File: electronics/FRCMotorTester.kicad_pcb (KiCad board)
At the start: 4 copper layers, 85.6 x 70.8 mm, 108 parts, among them J1 USB_B_Micro, J2 Conn_01x02_Socket, J3 Conn_01x03, J4 Conn_01x03, J5 Conn_01x03, J6 Conn_01x03, J7 Conn_ARM_JTAG_SWD_10, J8 Conn_01x02, J9 Conn_01x08, Q2 IRLML6401, SW1 PTS645SK50SMTR92LFS, SW2 RotaryEncoder_Switch, SW3 RotaryEncoder_Switch, U1 STM32F415RGTx, U2 TCAN1043xDxQ1, U4 USBLC6-2SC6, U5 LM1117DT-ADJ, U6 AOZ1280CI, U7 LM1117DT-ADJ, Y2 Crystal_GND24

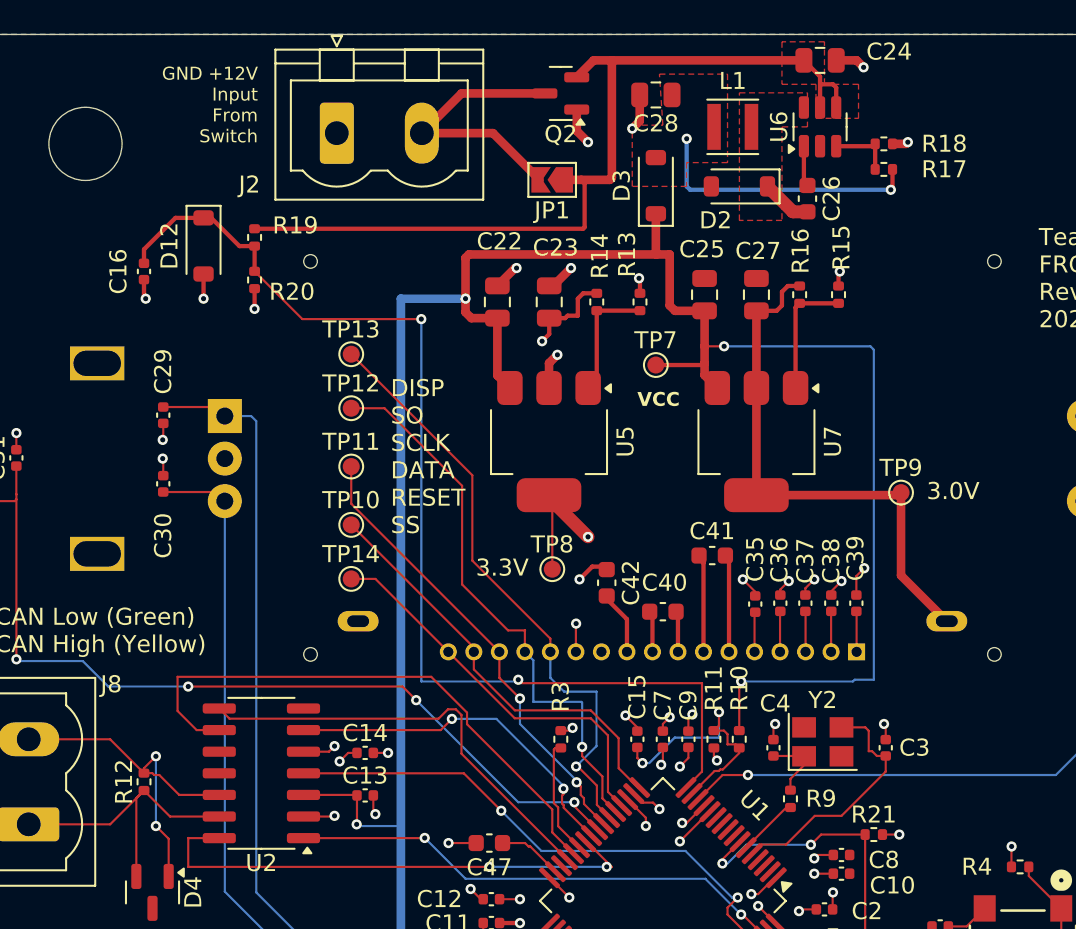
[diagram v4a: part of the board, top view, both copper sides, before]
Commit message: Tweaked parts to use Basic parts which are cheaper.
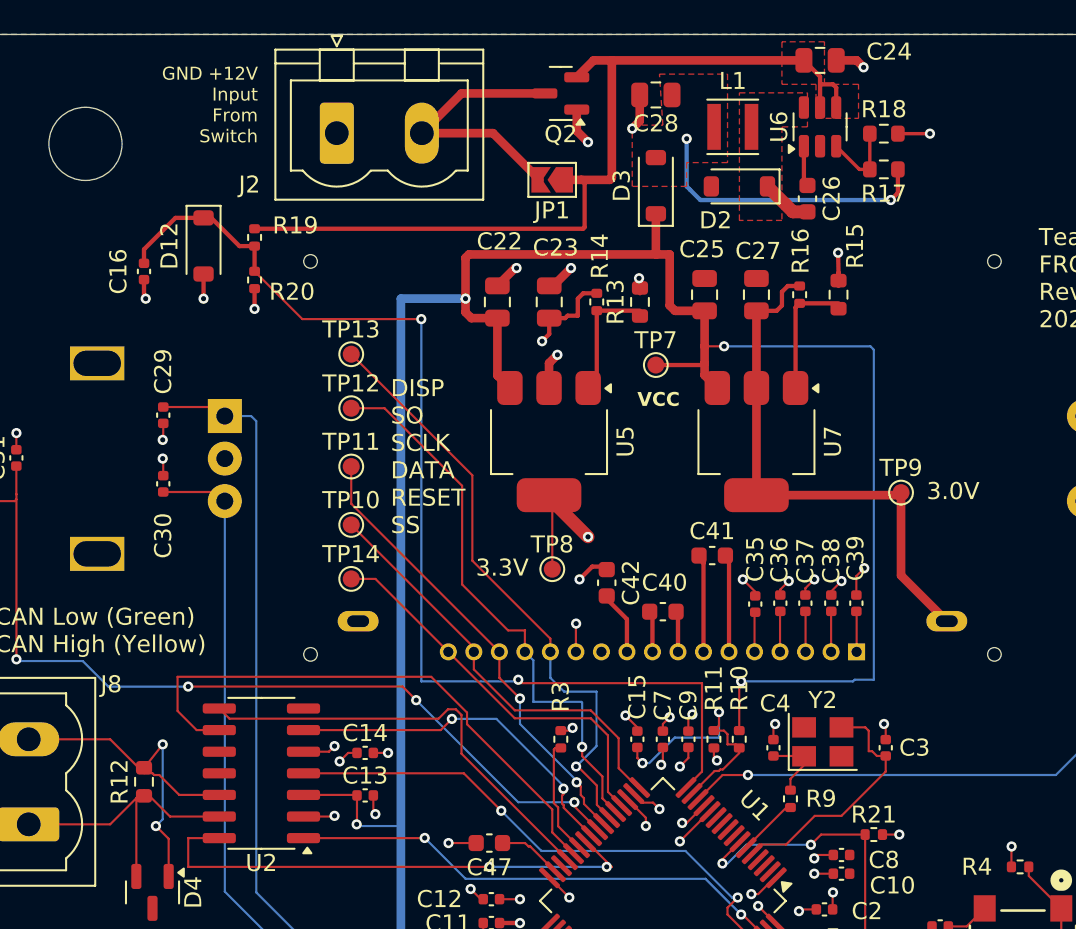
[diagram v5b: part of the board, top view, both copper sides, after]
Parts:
- R12, R13, R15, R17, R18: footprint Resistor_SMD:R_0402_1005Metric -> Resistor_SMD:R_0603_1608Metric
- moved R18 0.60 mm to (146.0, 41.9)
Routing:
- net GND: track 74.1 -> 76.1 mm
- net Net-(J8-Pin_2): track 21.2 -> 22.9 mm
- net Net-(D3-A): track 16.1 -> 17.1 mm
- net Net-(U6-FB): track 3.85 -> 4.64 mm

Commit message: Ordered this version.
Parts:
- SW1: footprint footprints:SW4_PTS645SK50SMTR92LFS_CNK -> footprints:PTS645SK50SMTR92LFS_CNK
- moved R4 2.50 mm to (154.0, 82.5)
- moved SW1 1.39 mm to (154.1, 89.3)
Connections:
- C17 pad 1: /Pico/BOOT -> BOOT
- DS1 pad 13: DISP_SO -> DISP_SI
- R2 pad 1: /Pico/BOOT -> BOOT
- SW1 pad 3: /Pico/BOOT -> BOOT
- SW1 pad 4: /Pico/BOOT -> BOOT
- TP13 pad 1: DISP_SO -> DISP_SI
- U1 pad 22: DISP_SO -> DISP_DATA
- U1 pad 23: DISP_DATA -> DISP_SI
- U1 pad 56: unconnected-(U1-PB4-Pad56) -> BOOT
- U1 pad 60: /Pico/BOOT -> BOOT
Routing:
- net DISP_SI: track 0.00 -> 36.0 mm, vias 0 -> 1
- net DISP_SO: track 35.7 -> 0.00 mm, vias 1 -> 0
- net BOOT: track 0.00 -> 30.2 mm
- net /Pico/BOOT: track 23.1 -> 0.00 mm
- net Net-(R4-Pad2): track 9.73 -> 14.1 mm

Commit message: Updated design for REV B.
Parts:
- removed C46: 2.2u, Capacitor_SMD:C_0603_1608Metric
- removed D7, D8: SP0502BAHT, Package_TO_SOT_SMD:SOT-23
- removed H2, H3, H4: MountingHole, MountingHole:MountingHole_4.3mm_M4
- removed J4, J5, J6: Conn_01x03, Connector_PinSocket_2.54mm:PinSocket_1x03_P2.54mm_Vertical
- removed J8: Conn_01x02, Connector_Phoenix_MSTB:PhoenixContact_MSTBVA_2,5_2-G_1x02_P5.00mm_Vertical
- removed U1: STM32F415RGTx, Package_QFP:LQFP-64_10x10mm_P0.5mm
- added J10: Conn_01x04, Connector_JST:JST_PH_S4B-PH-K_1x04_P2.00mm_Horizontal, F.Cu at (101.0, 43.5)
- added U3: STM32F446RETx, Package_QFP:LQFP-64_10x10mm_P0.5mm, F.Cu at (133.0, 87.0)
- C29, C30, C32, C33: value 0.1u -> 10n
- H1: footprint MountingHole:MountingHole_4.3mm_M4 -> footprints:brushless_buddy_logo
- J2: footprint Connector_Phoenix_MSTB:PhoenixContact_MSTBVA_2,5_2-G_1x02_P5.00mm_Vertical -> Connector_JST:JST_PH_S2B-PH-K_1x02_P2.00mm_Horizontal
- J3: value Conn_01x03 -> Conn_01x06; footprint Connector_PinSocket_2.54mm:PinSocket_1x03_P2.54mm_Vertical -> Connector_JST:JST_PH_S6B-PH-K_1x06_P2.00mm_Horizontal
- moved H1 91.5 mm to (169.2, 101.3)
- moved J3 32.0 mm to (167.7, 43.5), turned to 180 degrees
- moved J2 2.68 mm to (116.0, 43.5), turned to 180 degrees
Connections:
- D5 pad 2: 3V3 -> GENIO_02
- D6 pad 1: GENIO_02 -> GENIO_03
- D6 pad 2: 3V3 -> ANALOG_IN
- J3 pad 1: GND -> 3V3
- J3 pad 2: 3V3 -> GND
- J3 pad 3: ANALOG_IN -> GENIO_01
- U2 pad 10: unconnected-(U2-VSUP-Pad10) -> VCC
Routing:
- net GENIO_01: track 45.2 -> 96.0 mm
- net GENIO_02: track 49.5 -> 96.3 mm
- net Net-(J10-Pin_1): track 17.9 -> 59.6 mm
- net Net-(J10-Pin_2): track 22.9 -> 62.6 mm
- net GENIO_03: track 52.6 -> 92.3 mm
- net ANALOG_IN: track 41.3 -> 73.0 mm, vias 2 -> 3
- net VCC: track 148.1 -> 154.7 mm
- net /Power/VIN: track 16.3 -> 22.2 mm
- net 3V3: track 58.9 -> 54.0 mm, vias 31 -> 28
- net Net-(U1-VCAP_2): track 2.97 -> 0.00 mm
- net GND: track 76.1 -> 77.4 mm, vias 51 -> 56
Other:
- board text added: "+12V GND Input"
- board text added: "ANA GIO3 GIO2 GIO1 GND 3.3V"
- board text added: "CANL CANH CANL CANH"
- board text added: "Team 4360 and 7048 Brushless Buddy Rev B 2024"
- board text removed: "GND +12V Input From Switch"
- board text removed: "Team 4360 and 7048 FRC Motor Tester Rev A 2024"

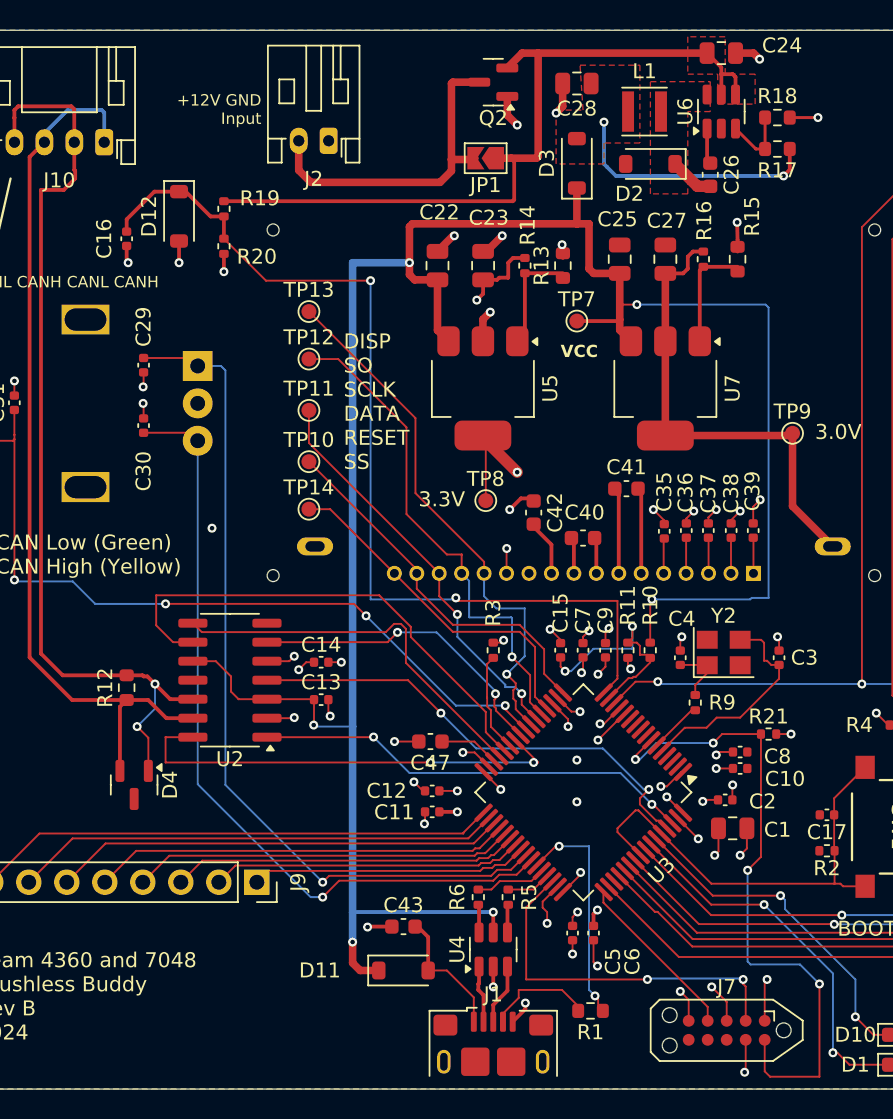
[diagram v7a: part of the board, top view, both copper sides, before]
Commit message: This version is working well. Need to figure out USB DFU programming.
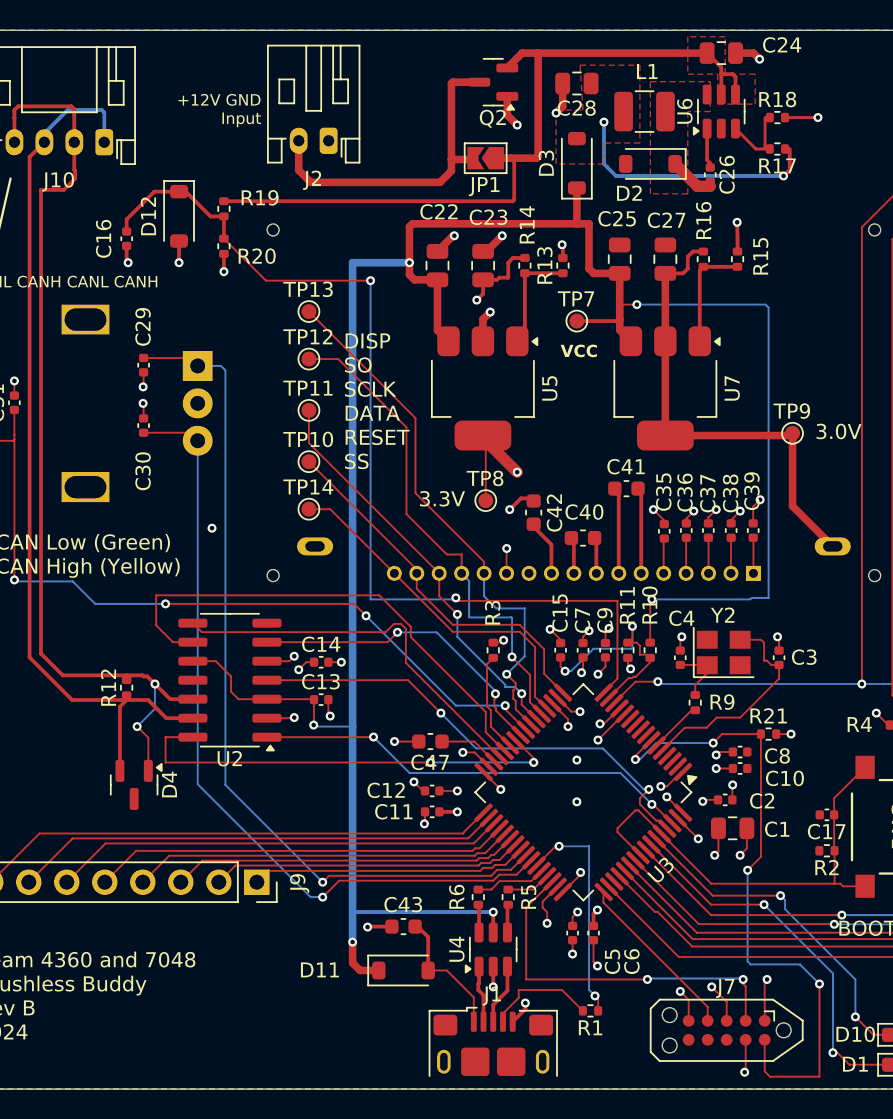
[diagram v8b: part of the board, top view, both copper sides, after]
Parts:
- C26: footprint Capacitor_SMD:C_0603_1608Metric -> Capacitor_SMD:C_0402_1005Metric
- L1: footprint Inductor_SMD:L_Taiyo-Yuden_MD-3030 -> Inductor_SMD:L_1210_3225Metric
- R1, R12, R13, R15, R17, R18: footprint Resistor_SMD:R_0603_1608Metric -> Resistor_SMD:R_0402_1005Metric
